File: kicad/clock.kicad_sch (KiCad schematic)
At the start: 183 parts, among them J1 USB4160-03-0230-C, J10 Knob: EM14 enc+SW (top face), J11 Radio-off toggle (rear), J12 NeoPixel ext (5V/DATA/GND, po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, J2 PROG, J3 Speaker DMA58-4 (4R), J6 DM3AT-SF-PEJM5, J7 Sensor board (BME688+TSL2591+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, J9 Wake COB 12V (warm+cool), M1 X40.879, Q1 2N7002, Q2 AO3401A, Q3 2N7002, Q4 AO3401A, Q6 AO3400A, Q7 AO3400A, Q8 2N7002, Q9 AO3401A, SW1 RESET, SW2 BOOT, U1 CH224K, U10 LTC4412ES6, U11 TB6612FNG, U12 TB6612FNG, U13 MCP23017, U14 QRE1113GR, U15 SN74AHCT1G125, U16 USBLC6-2SC6, U2 LT3652EMSE, U3 HY2111-GB, U4 AOSD32334C, U5 TPS61023, U6 TLV62569DBVR, U7 TPS55340PWPR, U8 ESP32-S3-WROOM-1-N8R8, U9 TAS5760MDAPR, Y1 32.768kHz

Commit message: sensor board v0.2: action kicad-sensor/REVIEW.md
Schematic, PCB, generators, QA checks and docs brought into one consistent
state. ERC 0 violations, DRC 0 violations / 0 unconnected / 0 parity issues,
gen/pcb_check.py 33/33, stamp_bom.py idempotent.

Safety and correctness
- #1  Address straps R3/R4/R10/R11 0R -> 10k. Fitting both halves of either
      pair shorted the MAIN board's +3V3 to GND through 0 ohm; it now costs
      330 uA and the part enumerates at a visible wrong address. PCB Value
      fields follow the schematic.
- W1  gen/pcb_build.py refuses to run without PCB_BUILD_WIPE_ROUTING=1. It
      produced the old 2-layer unrouted placement and would wipe the routing.
- #4  The reversed-harness / J10 mis-mate hazard is now a warning block on
      the schematic sheet, in README.md and on J10's own BOM line.

Versioning (#11) - one scheme in three places
- PCB title block added (there was none), schematic rev "A" -> "v0.2", silk
  SENSE v0.1 -> SENSE v0.2. pcb_check.py fails if the three disagree.

PCB (#7 #8 #10 #14)
- Thermal-island copper 21.0 -> 18.2 mm, GND share 8.8 -> 6.0 mm: the GND
  daisy-chain that ran down the inside of the island is replaced by the
  shortest exits that reach the pour.
- C4/C7 +0.175 mm east (all U1's and Y1's courtyards allow), restoring
  requirement 5 "nothing on the back behind U2".
- All five hidden reference designators un-hidden, the four stray free silk
  texts removed; only H1/H2 stay hidden, and that is now asserted.
- U3 moved to a project-local footprint fork,
  sensor:AMS_TSL25911FN_ALSWindow - the stock silk crosses the optical
  window 1.31 mm from the photodiode. Forked, not hand-edited, so Update
  Footprints from Library cannot undo it and DRC stays clean.

QA re-baselined (#6 #9 #15)
- pcb_check.py judged the generated 2-layer placement; four checks failed
  against a board that is fine. Clearance is now judged on pad-to-pad
  copper (>= 0.60 mm everywhere) with the six sub-0.22 mm courtyard pairs
  named a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
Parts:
- J10: Notes (none) -> Same part and same accepted 2.7 mm-tail deviation as J7 (ab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; Package JST ZH 1.50mm 6-pos TH vertical -> JST ZH 1.50mm 6-pos TH vertical, 2.7mm tail
- J11: Notes (none) -> Same accepted 2.7 mm-tail deviation as J7 (above); B2B-ZR-3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; Package JST ZH 1.50mm 2-pos TH vertical -> JST ZH 1.50mm 2-pos TH vertical, 2.7mm tail
- J7: Notes (none) -> 2.7 mm tail on a 1.6 mm board — JST specs 3.4 mm (B6B-ZR-3.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; Package JST ZH 1.50mm 6-pos TH vertical -> JST ZH 1.50mm 6-pos TH vertical, 2.7mm tail
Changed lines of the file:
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@@
 			)
 		)
-		(property "Package" "JST ZH 1.50mm 2-pos TH vertical"
+		(property "Notes" "Same accepted 2.7 mm-tail deviation as J7 (above); B2B-ZR-3.4 is not stocked either. 2 positions, so it cannot mis-mate with J7/J10"
+			(at 546.1 457.2 0)
+			(hide yes)
+			(show_name no)
+			(do_not_autoplace no)
+			(effects
+				(font
+					(size 1.27 1.27)
+				)
+			)
+		)
+		(property "Package" "JST ZH 1.50mm 2-pos TH vertical, 2.7mm tail"
 			(at 546.1 457.2 0)
 			(hide yes)
@@
 			)
 		)
-		(property "Package" "JST ZH 1.50mm 6-pos TH vertical"
+		(property "Notes" "2.7 mm tail on a 1.6 mm board — JST specs 3.4 mm (B6B-ZR-3.4) for this thickness, but that variant is made-to-order only (MOQ 2,000, 16 wk). Accepted deviation, see PCB_NOTES.md. Same part as the sensor board's J1: one harness, two identical ends"
+			(at 533.4 254 0)
+			(hide yes)
+			(show_name no)
+			(do_not_autoplace no)
+			(effects
+				(font
+					(size 1.27 1.27)
+				)
+			)
+		)
+		(property "Package" "JST ZH 1.50mm 6-pos TH vertical, 2.7mm tail"
 			(at 533.4 254 0)
 			(hide yes)
@@
 			)
 		)
-		(property "Package" "JST ZH 1.50mm 6-pos TH vertical"
+		(property "Notes" "Same part and same accepted 2.7 mm-tail deviation as J7 (above). MECHANICALLY IDENTICAL TO J7 AND 13.5 mm FROM IT — a ZHR-6 swapped between the two puts +5 V on the sensor board's +3V3 and destroys all three sensors. Label both harnesses"
+			(at 560.07 530.86 0)
+			(hide yes)
+			(show_name no)
+			(do_not_autoplace no)
+			(effects
+				(font
+					(size 1.27 1.27)
+				)
+			)
+		)
+		(property "Package" "JST ZH 1.50mm 6-pos TH vertical, 2.7mm tail"
 			(at 560.07 530.86 0)
 			(hide yes)

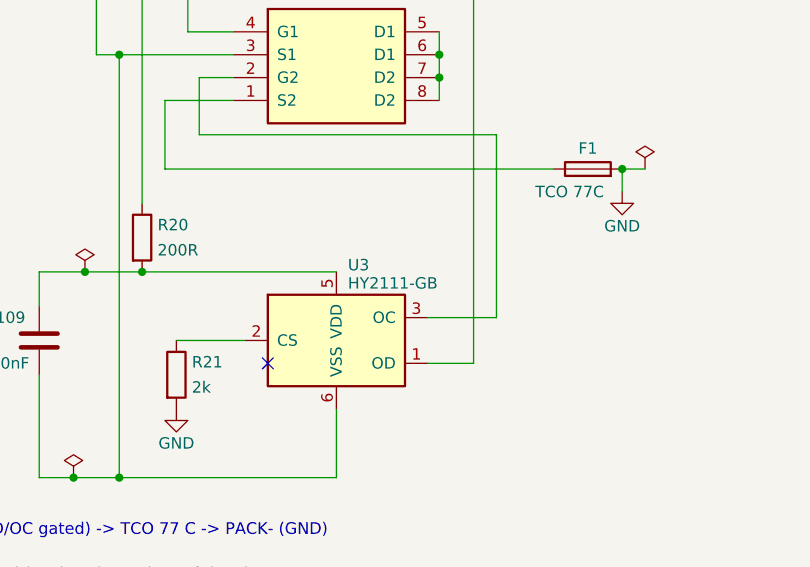
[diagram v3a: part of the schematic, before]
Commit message: protector -GB -> -HB; keep the 4 Ohm speaker, fix its rationale
Speaker: DMA58-4 (4 Ohm) confirmed, README §16 rationale corrected
That note claimed "8 Ohm would halve output to ~4 W". It would not, when
plugged - and plugged is the case that argument was made for. At 4 Ohm the
ceiling is not the rail, it is L5/L6 saturation: the rail would allow
16.5 W and the limiter caps it at 8 W to hold peak inductor current at 79 %
of Isat. At 8 Ohm you are rail-limited at 11.5 V -> 8.26 W, at 61 % of
Isat. Plugged, both impedances give ~8 W and the same SPL.

The 4 Ohm earns its place on BATTERY, where the rail does clip: 3.1 W vs
1.6 W, a real +3 dB. Plus the constants are already cut for it (-4.1 dBFS,
A_GAIN 19.2 dBV, L5/L6 10 uH - 8 Ohm wants 22 uH per TI, so it is two more
BOM lines, not a driver swap). Limiting in firmware is not a workaround, it
is the specified design: the limiter exists because nothing in hardware
protects L5/L6 (the amp's OCE trips at ~14 A in PBTL, 4-5x past Isat).

Protector: HY2111-GB -> HY2111-HB (REVIEW.md #6, closed)
Verified against battery_protector_hy2111.pdf p.190-201: the suffixes are
identical on every threshold - OV 4.28 / release 4.08 / OD 2.90 / release
3.00 - and differ only in discharge-OC V_DIP, 200 +/-25 mV vs 150 +/-25 mV.
Across the AOSD32334C pair that is a worst-case trip of 2.65 A instead of
1.89 A.

It matters because the rails hang off the BAT node and R18 caps the LT3652
at ~1 A, so the CELL supplies the balance even while plugged (#7's
corollary). A sunrise alarm - 8 W audio plus wake LEDs, ~12 W - pulls
~2.3 A from the cell. The -GB trips on that; the -HB does not.

Same SOT-23-6, same pinout, same R20/R21/C109 network, so this is a BOM
line. Applied at all three sources (parts_db.py, mksym.py's symbol default,
b_charger.py), regenerated, and carried into the routed PCB with
sync_pcb.py - 2 actions, 0 tracks cut. ERC 0, DRC 0, review_check 11/12,
all unchanged.

FIRMWARE.md §6.2 - new R-AUDIO-1
The audio section knew abo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
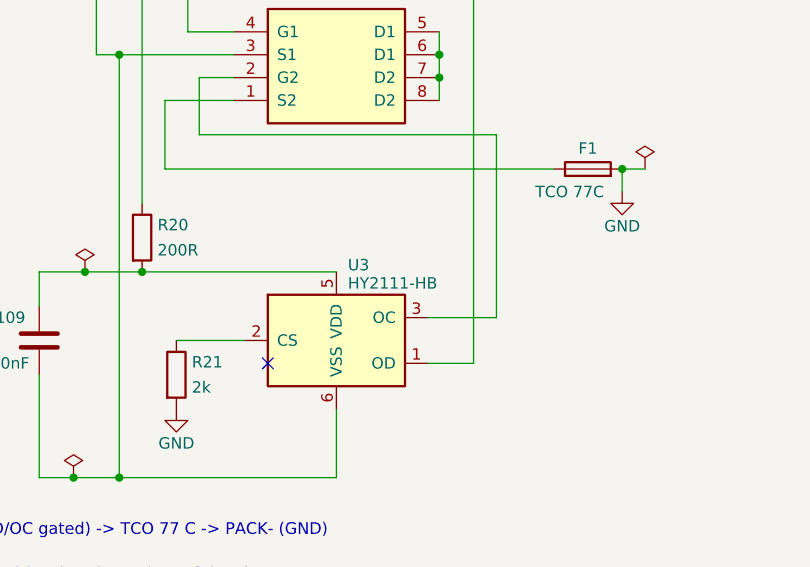
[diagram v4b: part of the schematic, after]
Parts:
- U3: value HY2111-GB -> HY2111-HB; MPN HY2111-GB -> HY2111-HB; Notes Not stocked at DigiKey - LCSC C82747 -> -HB suffix: discharge-OC V_DIP 200mV (the -GB's 150mV trips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
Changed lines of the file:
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@@
 			)
 		)
-		(property "Notes" "Same accepted 2.7 mm-tail deviation as J7 (above); B2B-ZR-3.4 is not stocked either. 2 positions, so it cannot mis-mate with J7/J10"
+		(property "Package" "JST ZH 1.50mm 2-pos TH vertical, 2.7mm tail"
 			(at 546.1 457.2 0)
 			(hide yes)
@@
 			)
 		)
-		(property "Package" "JST ZH 1.50mm 2-pos TH vertical, 2.7mm tail"
+		(property "MPN" "B2B-ZR(LF)(SN)"
 			(at 546.1 457.2 0)
 			(hide yes)
@@
 			)
 		)
-		(property "MPN" "B2B-ZR(LF)(SN)"
+		(property "Manufacturer" "JST Sales America"
 			(at 546.1 457.2 0)
 			(hide yes)
@@
 			)
 		)
-		(property "Manufacturer" "JST Sales America"
+		(property "Description" "CONN HEADER VERT 2POS 1.50MM"
 			(at 546.1 457.2 0)
 			(hide yes)
@@
 			)
 		)
-		(property "Description" "CONN HEADER VERT 2POS 1.50MM"
+		(property "Notes" "Same accepted 2.7 mm-tail deviation as J7 (above); B2B-ZR-3.4 is not stocked either. 2 positions, so it cannot mis-mate with J7/J10"
 			(at 546.1 457.2 0)
 			(hide yes)
@@
 			)
 		)
-		(property "Notes" "2.7 mm tail on a 1.6 mm board — JST specs 3.4 mm (B6B-ZR-3.4) for this thickness, but that variant is made-to-order only (MOQ 2,000, 16 wk). Accepted deviation, see PCB_NOTES.md. Same part as the sensor board's J1: one harness, two identical ends"
+		(property "Package" "JST ZH 1.50mm 6-pos TH vertical, 2.7mm tail"
 			(at 533.4 254 0)
 			(hide yes)
@@
 			)
 		)
-		(property "Package" "JST ZH 1.50mm 6-pos TH vertical, 2.7mm tail"
+		(property "MPN" "B6B-ZR(LF)(SN)"
 			(at 533.4 254 0)
 			(hide yes)
@@
 			)
 		)
-		(property "MPN" "B6B-ZR(LF)(SN)"
+		(property "Manufacturer" "JST Sales America"
 			(at 533.4 254 0)
 			(hide yes)
@@
 			)
 		)
-		(property "Manufacturer" "JST Sales America"
+		(property "Description" "CONN HEADER VERT 6POS 1.50MM"
 			(at 533.4 254 0)
 			(hide yes)
@@
 			)
 		)
-		(property "Description" "CONN HEADER VERT 6POS 1.50MM"
+		(property "Notes" "2.7 mm tail on a 1.6 mm board — JST specs 3.4 mm (B6B-ZR-3.4) for this thickness, but that variant is made-to-order only (MOQ 2,000, 16 wk). Accepted deviation, see PCB_NOTES.md. Same part as the sensor board's J1: one harness, two identical ends"
 			(at 533.4 254 0)
 			(hide yes)
@@
 			)
 		)
-		(property "Notes" "Same part and same accepted 2.7 mm-tail deviation as J7 (above). MECHANICALLY IDENTICAL TO J7 AND 13.5 mm FROM IT — a ZHR-6 swapped between the two puts +5 V on the sensor board's +3V3 and destroys all three sensors. Label both harnesses"
+		(property "Package" "JST ZH 1.50mm 6-pos TH vertical, 2.7mm tail"
 			(at 560.07 530.86 0)
 			(hide yes)
@@
 			)
 		)
-		(property "Package" "JST ZH 1.50mm 6-pos TH vertical, 2.7mm tail"
+		(property "MPN" "B6B-ZR(LF)(SN)"
 			(at 560.07 530.86 0)
 			(hide yes)
@@
 			)
 		)
-		(property "MPN" "B6B-ZR(LF)(SN)"
+		(property "Manufacturer" "JST Sales America"
 			(at 560.07 530.86 0)
 			(hide yes)
@@
 			)
 		)
-		(property "Manufacturer" "JST Sales America"
+		(property "Description" "CONN HEADER VERT 6POS 1.50MM"
 			(at 560.07 530.86 0)
 			(hide yes)
@@
 			)
 		)
-		(property "Description" "CONN HEADER VERT 6POS 1.50MM"
+		(property "Notes" "Same part and same accepted 2.7 mm-tail deviation as J7 (above). MECHANICALLY IDENTICAL TO J7 AND 13.5 mm FROM IT — a ZHR-6 swapped between the two puts +5 V on the sensor board's +3V3 and destroys all three sensors. Label both harnesses"
 			(at 560.07 530.86 0)
 			(hide yes)
@@
 			)
 		)
-		(property "Value" "HY2111-GB"
+		(property "Value" "HY2111-HB"
 			(at 81.28 270.51 0)
 			(show_name no)
@@
 			)
 		)
-		(property "MPN" "HY2111-GB"
+		(property "MPN" "HY2111-HB"
 			(at 80.01 276.86 0)
 			(hide yes)
@@
 			)
 		)
-		(property "Notes" "Not stocked at DigiKey - LCSC C82747"
+		(property "Notes" "-HB suffix: discharge-OC V_DIP 200mV (the -GB's 150mV trips on a loud plugged alarm, REVIEW.md #6). All other thresholds identical to -GB. Not stocked at DigiKey - LCSC C82747 is the -GB; order the -HB variant explicitly and CHECK THE MARKING on arrival"
 			(at 80.01 276.86 0)
 			(hide yes)

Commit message: bom: C172's MPN was never real, and U3 ships as a -GB
PCBWay's first assembly quote (T-1N10W1120006A, 1 unit) flagged six BOM
lines. Two of them change the design record.

C172 was `EEH-ZA1E101P`, which does not exist -- the ZA series uses the
plain -P suffix only at other voltages/values (EEH-ZA1H101P is the 50 V
part, EEH-ZA1E560P the 56 uF one). The 25 V / 100 uF part is
`EEH-ZA1E101XP`, in stock at LCSC C264047 and DigiKey 3088115. Fixed in
parts_db.py and re-stamped; only C172's MPN + Notes moved in the schematic
and the PCB. The note's own ripple figure was wrong too -- 2 A @100 kHz
with 30 mOhm ESR, not ~1.3 A / ~40 mOhm -- so #19's rule is met 3x.

U3 goes back to HY2111-GB: -HB is out of stock (LCSC C160793) and our own
BOM note pointed the assembler at C82747, which *is* the -GB. So REVIEW.md
#6 is closed by firmware on this build instead of by the part: R-AUDIO-1
grew a -GB budget (hold peak cell current under ~1.8 A -- 8 W audio or the
sunrise LED ramp, never both), and bring-up has to read the marking on U3
rather than trust the BOM.

F1 (77 C one-shot TCO) and M1 (movement) ship unpopulated, both deliberate.
F1 means the safety chain is incomplete as delivered: no cell in the holder
until it is hand-soldered in.

Co-Authored-By: Claude Opus 5 <noreply@anthropic.com>
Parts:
- C172: MPN EEH-ZA1E101P -> EEH-ZA1E101XP; Notes PVDD bulk. **Hybrid polymer, NOT a plain electrolytic** -- the ripple rating is the spec that matters here, not the value. A class-D BTL draws i_supply = P/PVDD x (1-cos 2wt), so the bulk sees (P/PVDD)/sqrt(2) rms at twice the audio frequency: 0.49 A at the 8 W firmware limit, 0.68 A at clip. The previous part (Rubycon 25TZV100M6.3X8, 300 mA @100 kHz) was under-rated ~1.6x; the ZA hybrid is ~1.3 A with ~40 mOhm ESR, and 7.7 mm actually fits the CP_Elec_6.3x7.7 land better than the old 8.0 mm can. SUBSTITUTION RULE: any D6.3 part with >=600 mA @100 kHz ripple and >=25 V. Value may drop to 68 uF if that buys the rating. VERIFY DigiKey stock before ordering (REVIEW.md #19) -> PVDD bulk. **Hybrid polymer, NOT a plain electrolytic** -- the ripple rating is the spec that matters here, not the value. A class-D BTL draws i_supply = P/PVDD x (1-cos 2wt), so the bulk sees (P/PVDD)/sqrt(2) rms at twice the audio frequency: 0.49 A at the 8 W firmware limit, 0.68 A at clip. The previous part (Rubycon 25TZV100M6.3X8, 300 mA @100 kHz) was under-rated ~1.6x; the ZA hybrid is 2 A @100 kHz with 30 mOhm ESR (Panasonic/DigiKey attributes), on the same CP_Elec_6.3x7.7 land -- D6.3 pads are diameter-driven, so an 8.0 mm can drops in too. SUBSTITUTION RULE: any D6.3 part with >=600 mA @100 kHz ripple and >=25 V. Value may drop to 68 uF if that buys the rating. Stock verified 2026-08-10: LCSC C264047, DigiKey 3088115 (REVIEW.md #19)
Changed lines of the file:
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@@
 			)
 		)
-		(property "MPN" "EEH-ZA1E101P"
+		(property "MPN" "EEH-ZA1E101XP"
 			(at 751.84 293.37 0)
 			(hide yes)
@@
 			)
 		)
-		(property "Notes" "PVDD bulk. **Hybrid polymer, NOT a plain electrolytic** -- the ripple rating is the spec that matters here, not the value. A class-D BTL draws i_supply = P/PVDD x (1-cos 2wt), so the bulk sees (P/PVDD)/sqrt(2) rms at twice the audio frequency: 0.49 A at the 8 W firmware limit, 0.68 A at clip. The previous part (Rubycon 25TZV100M6.3X8, 300 mA @100 kHz) was under-rated ~1.6x; the ZA hybrid is ~1.3 A with ~40 mOhm ESR, and 7.7 mm actually fits the CP_Elec_6.3x7.7 land better than the old 8.0 mm can. SUBSTITUTION RULE: any D6.3 part with >=600 mA @100 kHz ripple and >=25 V. Value may drop to 68 uF if that buys the rating. VERIFY DigiKey stock before ordering (REVIEW.md #19)"
+		(property "Notes" "PVDD bulk. **Hybrid polymer, NOT a plain electrolytic** -- the ripple rating is the spec that matters here, not the value. A class-D BTL draws i_supply = P/PVDD x (1-cos 2wt), so the bulk sees (P/PVDD)/sqrt(2) rms at twice the audio frequency: 0.49 A at the 8 W firmware limit, 0.68 A at clip. The previous part (Rubycon 25TZV100M6.3X8, 300 mA @100 kHz) was under-rated ~1.6x; the ZA hybrid is 2 A @100 kHz with 30 mOhm ESR (Panasonic/DigiKey attributes), on the same CP_Elec_6.3x7.7 land -- D6.3 pads are diameter-driven, so an 8.0 mm can drops in too. SUBSTITUTION RULE: any D6.3 part with >=600 mA @100 kHz ripple and >=25 V. Value may drop to 68 uF if that buys the rating. Stock verified 2026-08-10: LCSC C264047, DigiKey 3088115 (REVIEW.md #19)"
 			(at 751.84 293.37 0)
 			(hide yes)
